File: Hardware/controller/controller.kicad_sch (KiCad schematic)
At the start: 17 parts, among them J101 Conn_02x10_Odd_Even, U101 PCA9543A

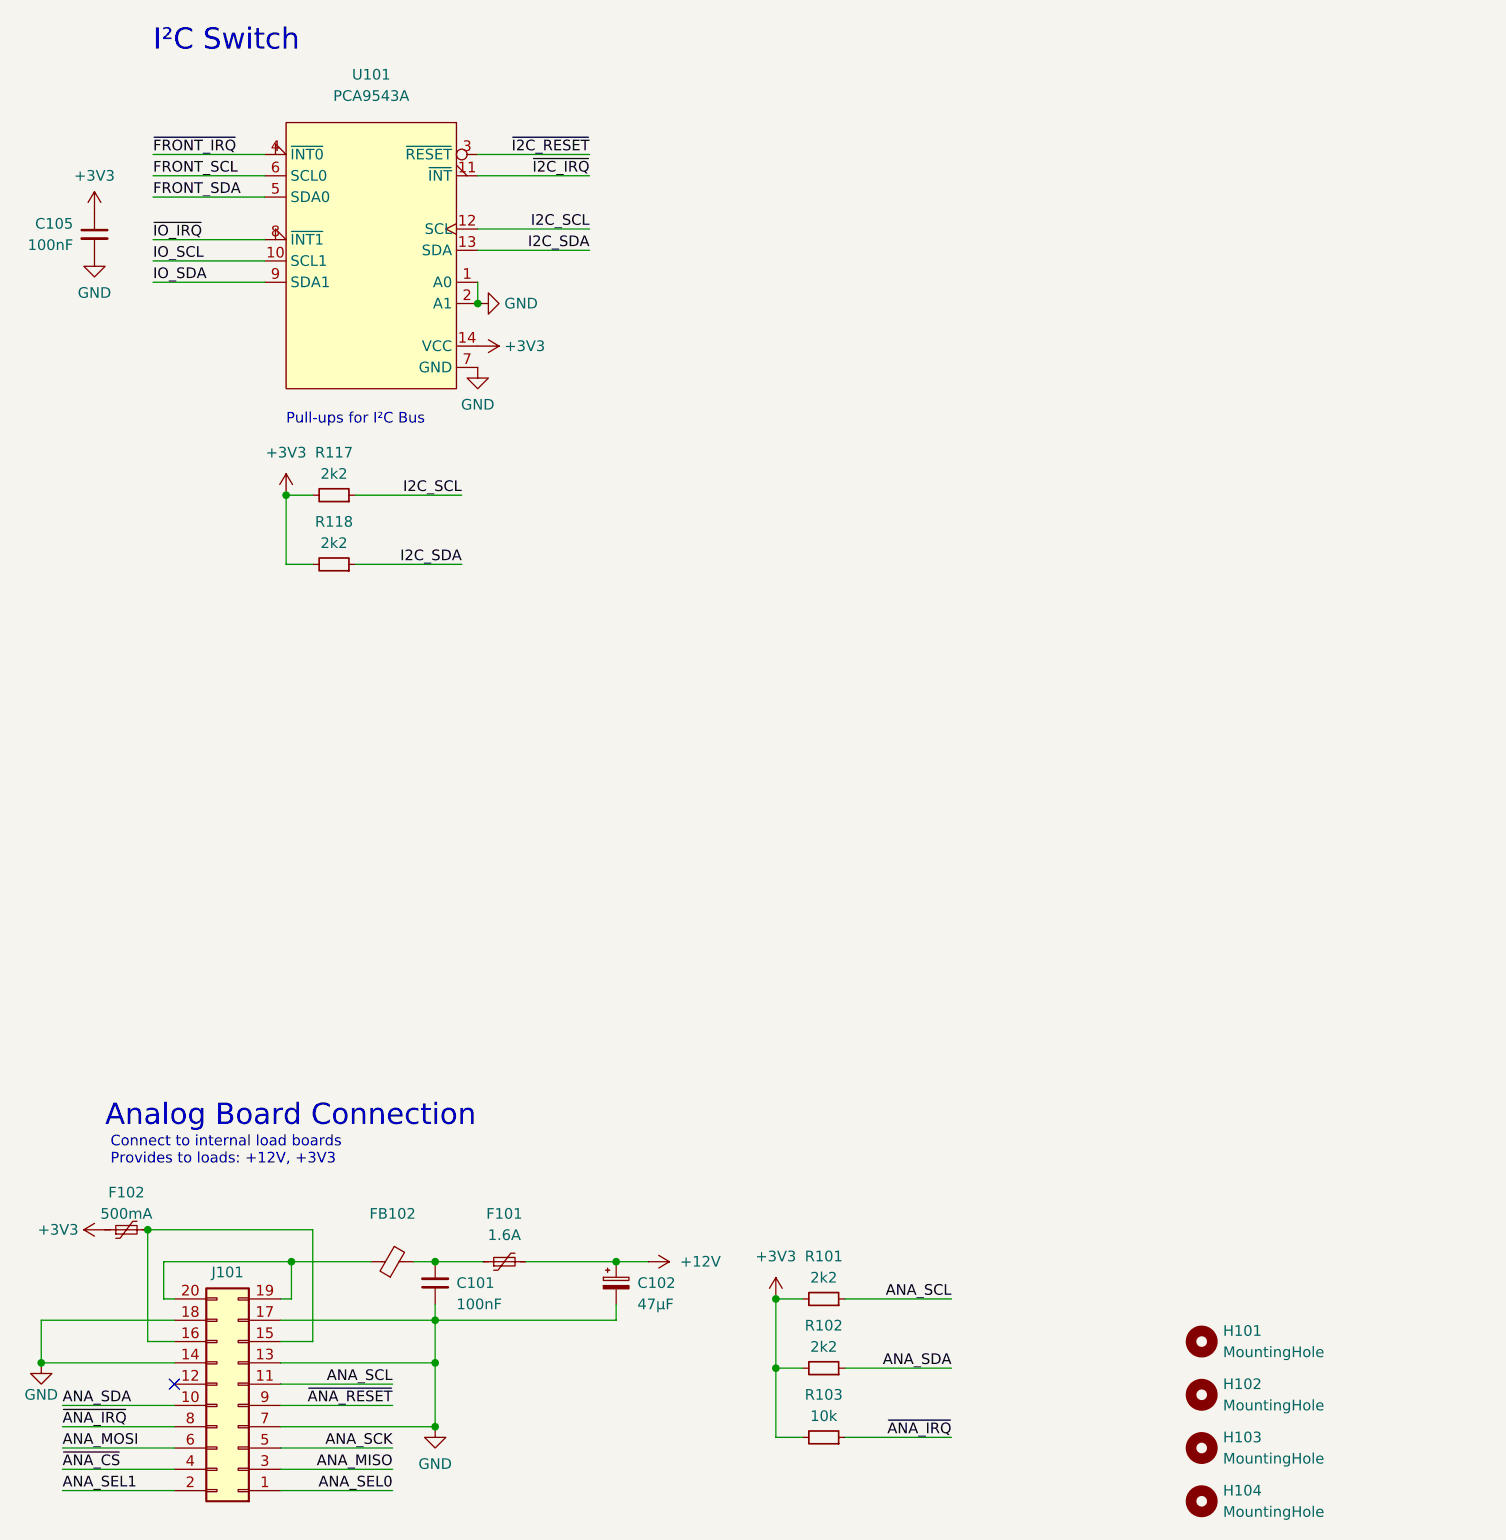
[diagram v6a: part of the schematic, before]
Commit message: Begin cleaning up controller for rework
- Removed some of the old stuff

- Added USB host connector for front panel (including footprint for new
  ESD boi)
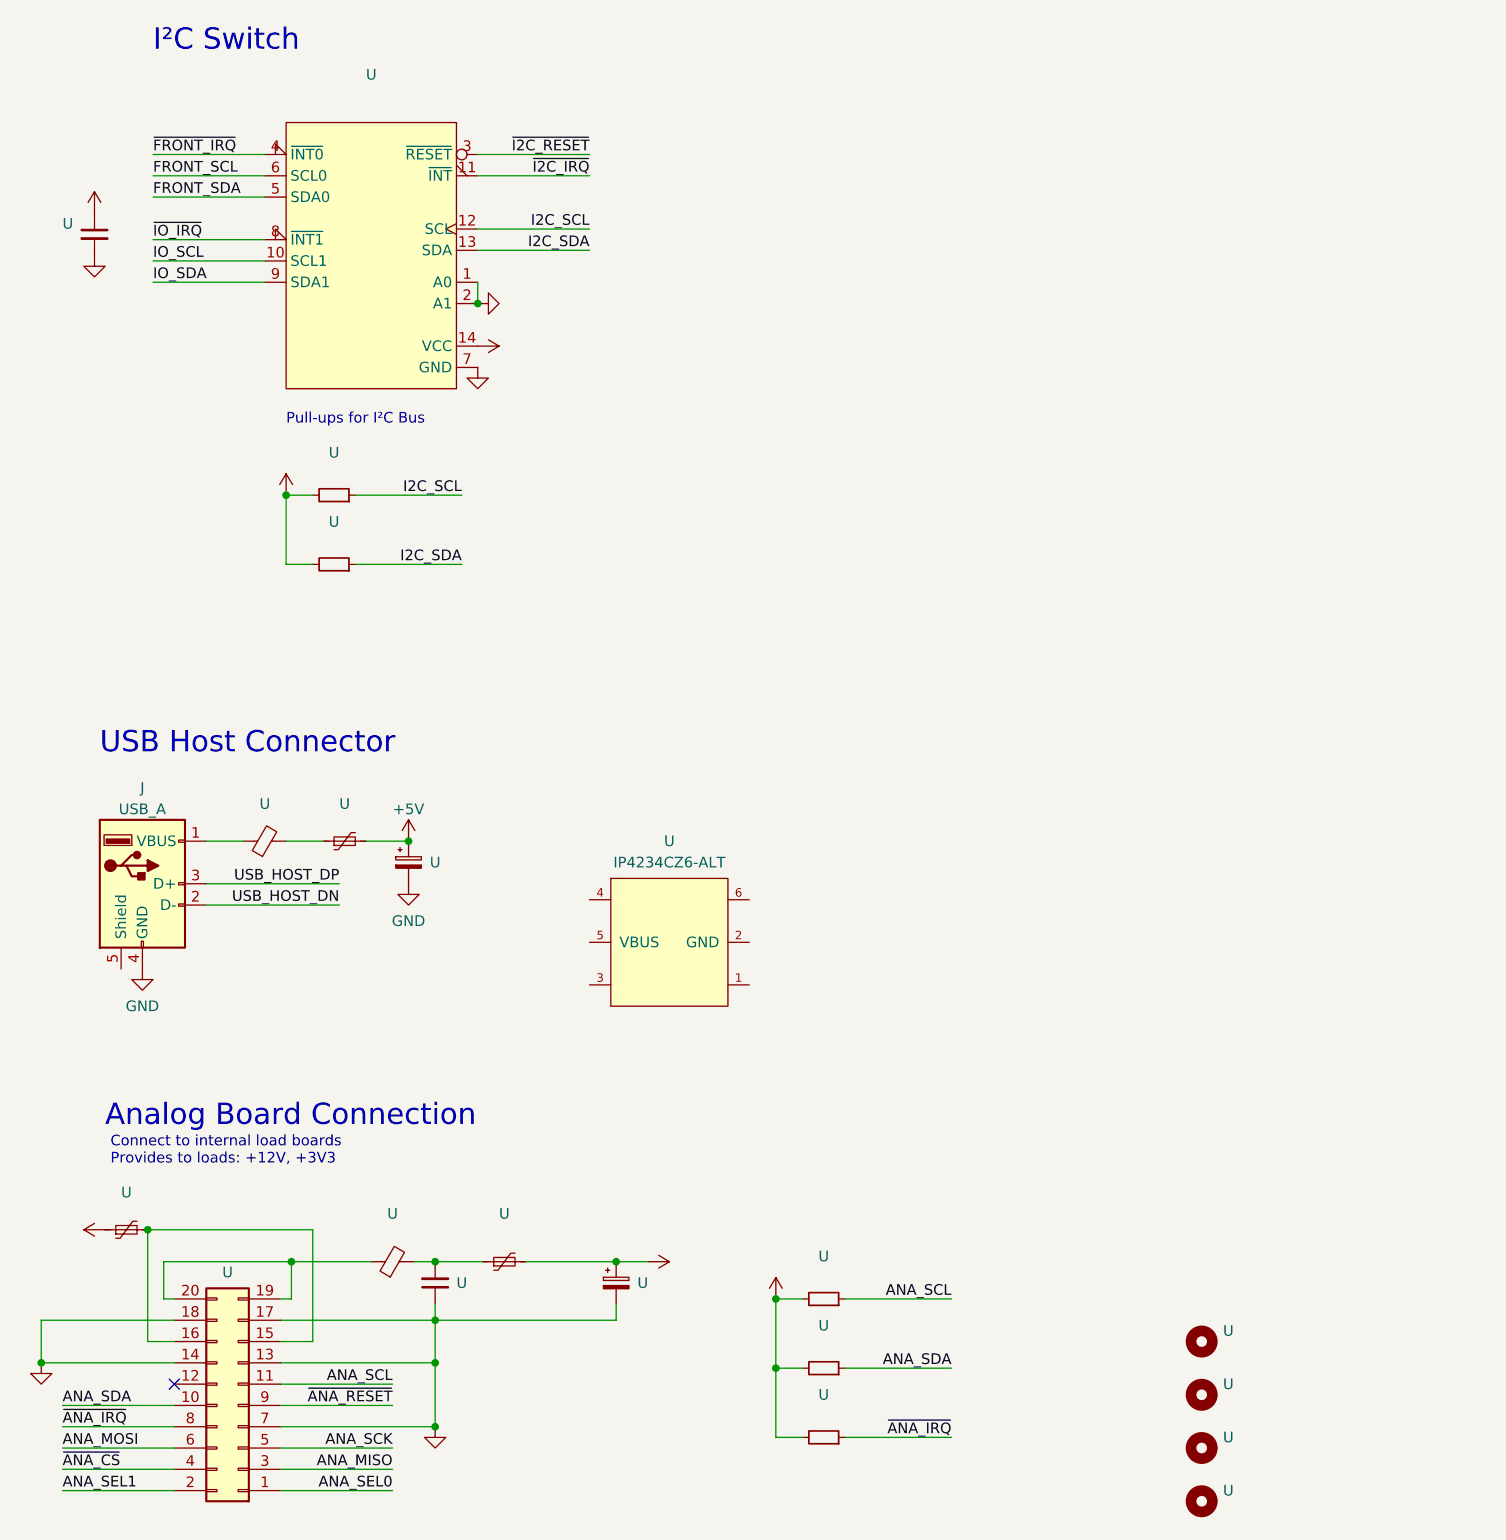
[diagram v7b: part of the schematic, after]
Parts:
- added J: USB_A, symbol Connector:USB_A
- added U: (no value), symbol Device:Polyfuse_Small
- added U: (no value), symbol Device:C_Polarized_Small
- added U: IP4234CZ6-ALT, Package_SO:TSOP-6_1.65x3.05mm_P0.95mm, symbol programmable-load:IP4234CZ6-ALT
- added U: (no value), symbol Device:FerriteBead_Small
- U: renamed from R118; value 2k2 -> (none); footprint Resistor_SMD:R_0805_2012Metric_Pad1.20x1.40mm_HandSolder -> (none)
- U: renamed from R101; value 2k2 -> (none); footprint Resistor_SMD:R_0805_2012Metric_Pad1.20x1.40mm_HandSolder -> (none)
- U: renamed from H101; value MountingHole -> (none); footprint MountingHole:MountingHole_3.2mm_M3 -> (none)
- U: renamed from C105; value 100nF -> (none); footprint Capacitor_SMD:C_0805_2012Metric_Pad1.18x1.45mm_HandSolder -> (none)
- U: renamed from R102; value 2k2 -> (none); footprint Resistor_SMD:R_0805_2012Metric_Pad1.20x1.40mm_HandSolder -> (none)
- U: renamed from C101; value 100nF -> (none); footprint Capacitor_SMD:C_0805_2012Metric_Pad1.18x1.45mm_HandSolder -> (none)
- U: renamed from U101; value PCA9543A -> (none); footprint Package_SO:TSSOP-14_4.4x5mm_P0.65mm -> (none)
- U: renamed from F102; value 500mA -> (none); footprint Fuse:Fuse_1206_3216Metric_Pad1.42x1.75mm_HandSolder -> (none)
- U: renamed from F101; value 1.6A -> (none); footprint Fuse:Fuse_1812_4532Metric_Pad1.30x3.40mm_HandSolder -> (none)
- U: renamed from H102; value MountingHole -> (none); footprint MountingHole:MountingHole_3.2mm_M3 -> (none)
- U: renamed from H103; value MountingHole -> (none); footprint MountingHole:MountingHole_3.2mm_M3 -> (none)
- U: renamed from J101; value Conn_02x10_Odd_Even -> (none); footprint Connector_IDC:IDC-Header_2x10_P2.54mm_Horizontal -> (none)
- U: renamed from R117; value 2k2 -> (none); footprint Resistor_SMD:R_0805_2012Metric_Pad1.20x1.40mm_HandSolder -> (none)
- U: renamed from R103; value 10k -> (none); footprint Resistor_SMD:R_0805_2012Metric_Pad1.20x1.40mm_HandSolder -> (none)
- U: renamed from H104; value MountingHole -> (none); footprint MountingHole:MountingHole_3.2mm_M3 -> (none)
- U: renamed from C102; value 47µF -> (none); footprint Capacitor_SMD:CP_Elec_6.3x5.4 -> (none); MPN 865060343004 -> EMVA250ADA470MF55G
- U: renamed from FB102; value FerriteBead_Small -> (none); footprint Resistor_SMD:R_0805_2012Metric_Pad1.20x1.40mm_HandSolder -> (none)
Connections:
- net GND: now also J.4 (GND), U.2
- new net: U.1, U.2
- new net: J.1 (VBUS), U.1
- new net +5V: U.1, U.2
- new net USB_HOST_DN: J.2 (D-)
- new net USB_HOST_DP: J.3 (D+)
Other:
- note added: "USB Host Connector"

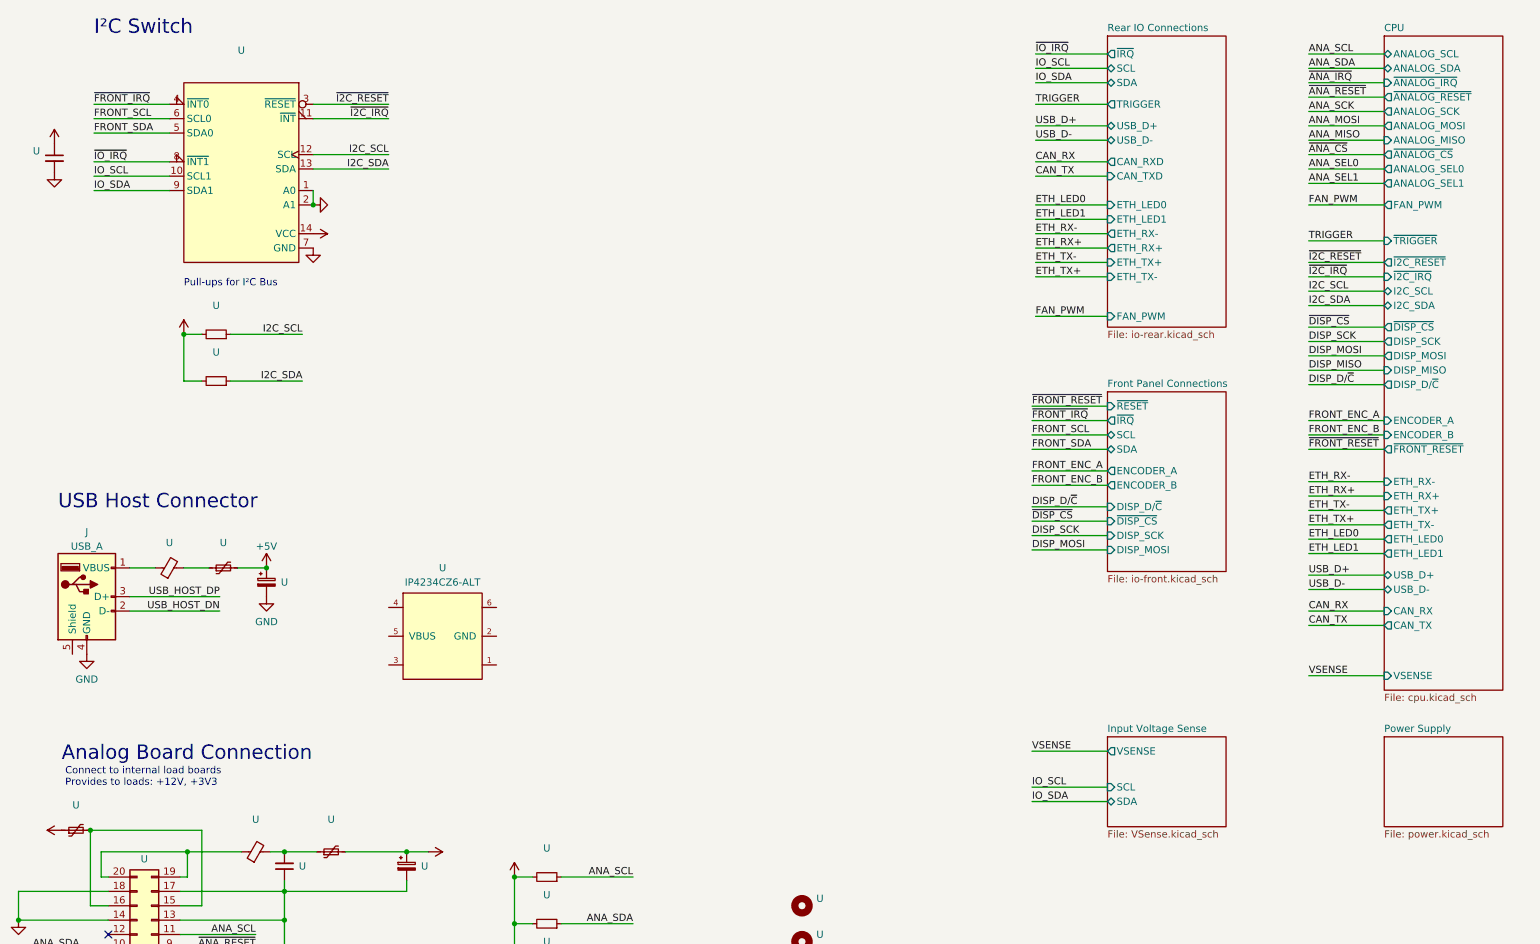
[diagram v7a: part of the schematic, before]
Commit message: More work on controller; add MYIR SoM footprint
- Begin cleaning up the controller board, that is removing all of the
  old CPU stuff and replacing it with new stuff, and general cleanup

- Create a footprint for the STM32MP1 SoM (MYR MYC-YA151C family)
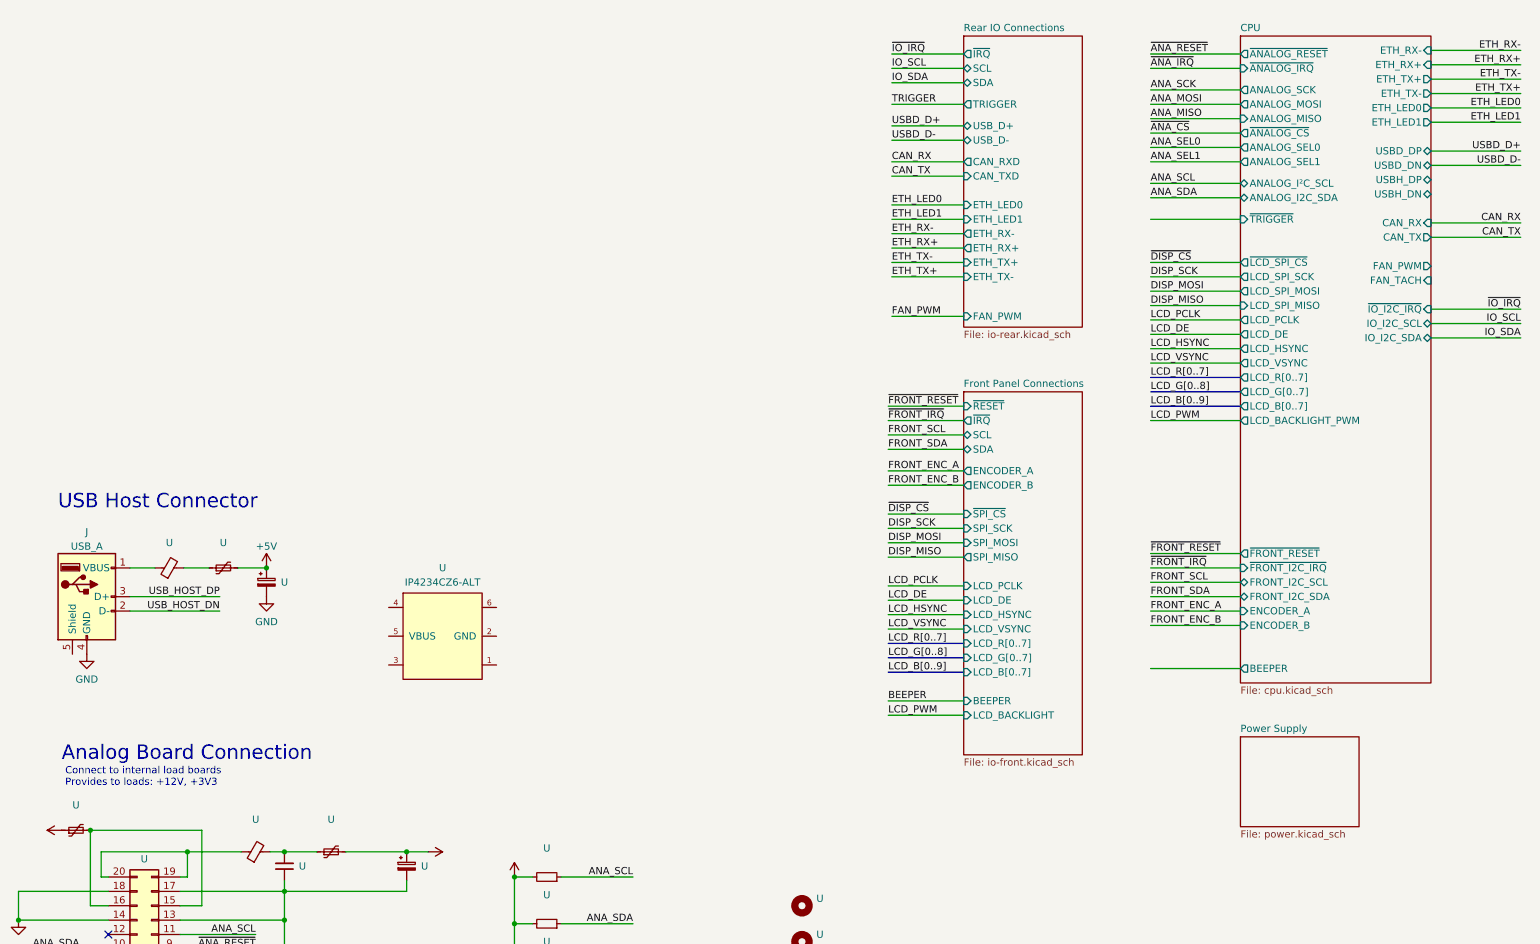
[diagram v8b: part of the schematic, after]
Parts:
- removed U (x2): (no value), symbol Device:R_Small
- removed U: (no value), symbol Device:C_Small
- removed U: (no value), symbol programmable-load:PCA9543A
- J: MPN (none) -> UJ2-AH-4-TH
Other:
- removed sheet Input Voltage Sense
- sheet CPU ports: added ANALOG_I2C_SDA, ANALOG_I²C_SCL, BEEPER, FAN_TACH, FRONT_I2C_SCL, FRONT_I2C_SDA, IO_I2C_SCL, IO_I2C_SDA, LCD_BACKLIGHT_PWM, LCD_B[0..7], LCD_DE, LCD_G[0..7], LCD_HSYNC, LCD_PCLK, LCD_R[0..7], LCD_SPI_MISO, LCD_SPI_MOSI, LCD_SPI_SCK, LCD_VSYNC, USBD_DN, USBD_DP, USBH_DN, USBH_DP, ~{FRONT_I2C_IRQ}, ~{IO_I2C_IRQ}, ~{LCD_SPI_CS}; removed ANALOG_SCL, ANALOG_SDA, DISP_D/~{C}, DISP_MISO, DISP_MOSI, DISP_SCK, I2C_SCL, I2C_SDA, USB_D+, USB_D-, VSENSE, ~{DISP_CS}, ~{I2C_IRQ}, ~{I2C_RESET}
- sheet Front Panel Connections ports: added BEEPER, LCD_BACKLIGHT, LCD_B[0..7], LCD_DE, LCD_G[0..7], LCD_HSYNC, LCD_PCLK, LCD_R[0..7], LCD_VSYNC, SPI_MISO, SPI_MOSI, SPI_SCK, ~{SPI_CS}; removed DISP_D/~{C}, DISP_MOSI, DISP_SCK, ~{DISP_CS}
- note removed: "I²C Switch"
- note removed: "Pull-ups for I²C Bus"
